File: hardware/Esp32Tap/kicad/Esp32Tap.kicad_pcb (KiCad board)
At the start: 4 copper layers, 100 x 55 mm, 93 parts, among them J1 RJ45_Console_54602-908LF, J2 RJ45_Motor_54602-908LF, J3 USB-C_HRO_TYPE-C-31-M-12, K1 G6K-2F-Y-TR DC5, Q1 BC817-40,215, Q2 2N7002, SW1 KMR2-EN, SW2 KMR2-BOOT, U1 ESP32-S3-WROOM-1-N8, U2 TPS54202DDCR, U3 USBLC6-2SC6, U4 TPS3700DDCR, U5 TPS70950DBVR, U6 SN74LVC2G08DCTR, U7 SN74LVC1G126DBVR

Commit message: hardware: clear residual JLC DFM findings
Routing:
- net PIN4_PASS: track 39.1 -> 36.0 mm, vias 4 -> 3
- net PIN3: track 110.3 -> 108.1 mm
- net EN: track 100.5 -> 102.0 mm, vias 9 -> 8

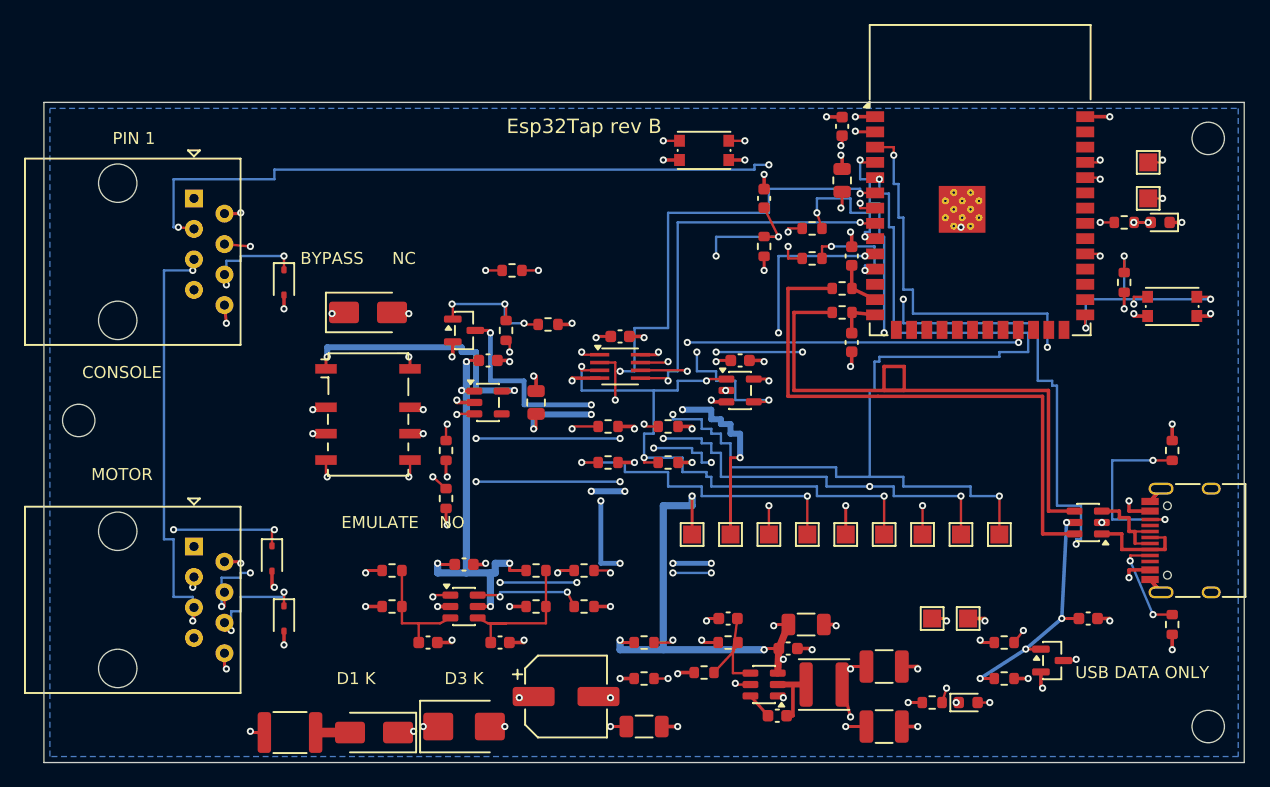
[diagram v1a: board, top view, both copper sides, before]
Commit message: hardware: publish body-safe fabrication legend
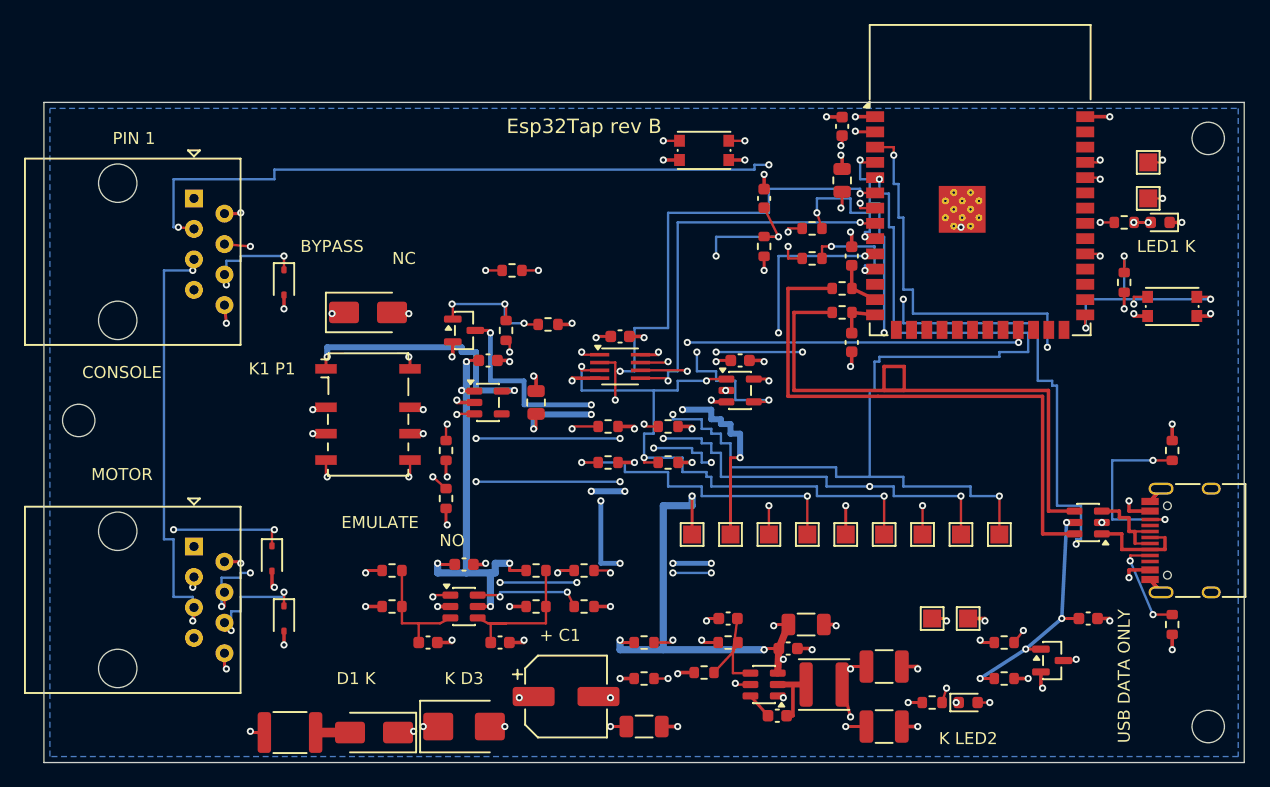
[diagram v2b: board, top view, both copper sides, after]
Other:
- board text added: "+ C1"
- board text added: "K D3"
- board text added: "K LED2"
- board text added: "K1 P1"
- board text added: "LED1 K"
- board text removed: "D3 K"
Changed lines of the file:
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@@
+		)
+	)
+	(gr_text "K1 P1"
+		(at 119 122.2 0)
+		(layer "F.SilkS")
+		(effects
+			(font
+				(size 1 1)
+				(thickness 0.2)
+			)
 		)
 	)
 	(gr_text "BYPASS"
-		(at 124 113 0)
+		(at 124 112 0)
 		(layer "F.SilkS")
 		(effects
@@
 	)
 	(gr_text "NO"
-		(at 134 135 0)
+		(at 134 136.5 0)
 		(layer "F.SilkS")
 		(effects
@@
 		)
 	)
-	(gr_text "D3 K"
+	(gr_text "K D3"
 		(at 135 148 0)
 		(layer "F.SilkS")
@@
 		)
 	)
-	(gr_text "USB DATA ONLY"
-		(at 191.5 147.5 0)
+	(gr_text "+ C1"
+		(at 143 144.4 0)
 		(layer "F.SilkS")
 		(effects
+			(font
+				(size 1 1)
+				(thickness 0.2)
+			)
+		)
+	)
+	(gr_text "K LED2"
+		(at 177 153 0)
+		(layer "F.SilkS")
+		(effects
+			(font
+				(size 1 1)
+				(thickness 0.2)
+			)
+		)
+	)
+	(gr_text "LED1 K"
+		(at 193.5 112 0)
+		(layer "F.SilkS")
+		(effects
+			(font
+				(size 1 1)
+				(thickness 0.2)
+			)
+		)
+	)
+	(gr_text "USB DATA ONLY"
+		(at 190 147.8 90)
+		(layer "F.SilkS")
+		(effects

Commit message: hardware: redesign Esp32Tap as compact turnkey Rev C (#52)
Redesign the serial-powered Esp32Tap around compact SMT Micro-Fit harness interfaces, regenerate and validate the PCB/enclosure/manufacturing package, and add fail-closed evidence, ngspice, vendor, and handoff documentation.

The hardware remains HOLD pending live JLC process/quote confirmation and physical installed measurements.
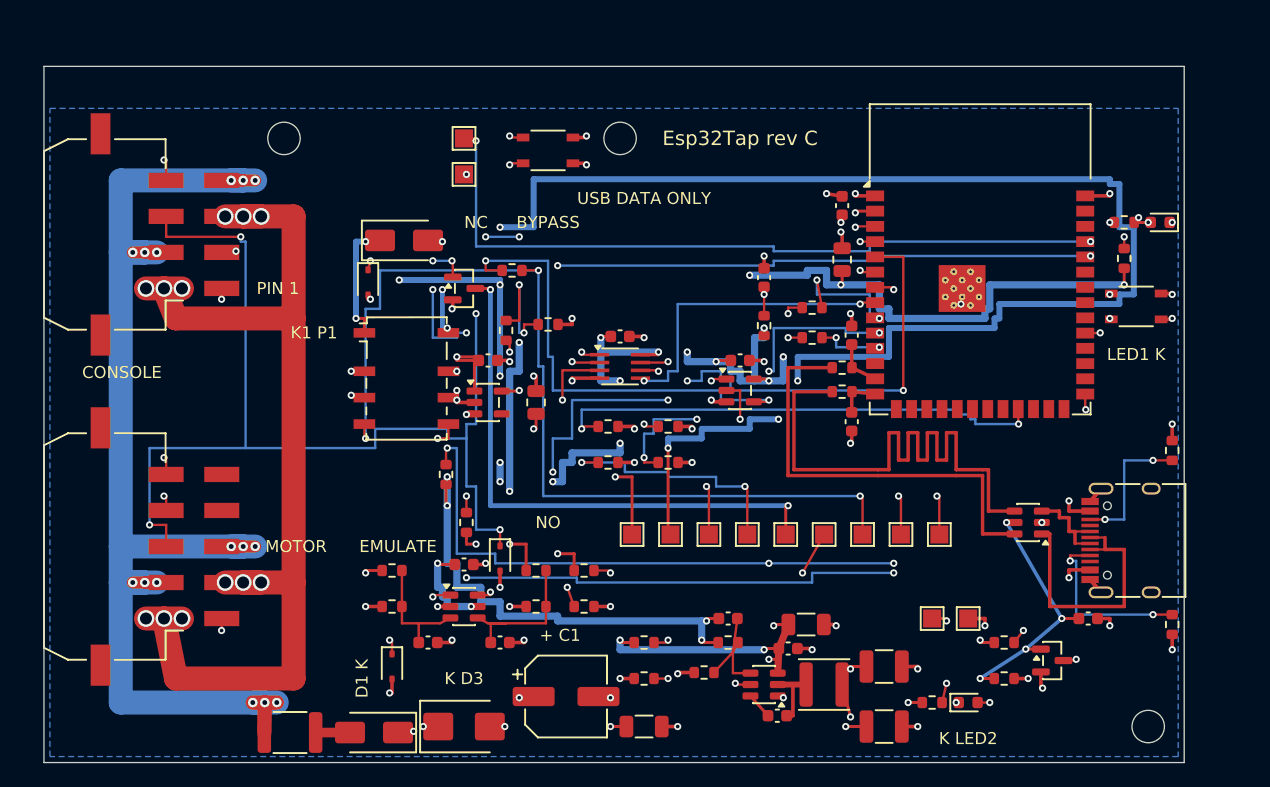
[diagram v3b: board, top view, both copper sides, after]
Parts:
- J1: value RJ45_Console_54602-908LF -> 430450809; footprint Connector_RJ:RJ45_Amphenol_54602-x08_Horizontal -> Connector_Molex:Molex_Micro-Fit_3.0_43045-0809_2x04-1MP_P3.00mm_Horizontal
- J2: value RJ45_Motor_54602-908LF -> 430451010; footprint Connector_RJ:RJ45_Amphenol_54602-x08_Horizontal -> Connector_Molex:Molex_Micro-Fit_3.0_43045-1010_2x05-1MP_P3.00mm_Horizontal
- SW1: value KMR2-EN -> SKRPACE010; footprint Button_Switch_SMD:SW_Push_1P1T_NO_CK_KMR2 -> Button_Switch_SMD:SW_SPST_SKRPACE010
- SW2: value KMR2-BOOT -> SKRPACE010; footprint Button_Switch_SMD:SW_Push_1P1T_NO_CK_KMR2 -> Button_Switch_SMD:SW_SPST_SKRPACE010
- moved TP1 57.0 mm to (135.0, 103.0)
- moved TP2 57.0 mm to (135.0, 106.0)
- moved MH2 49.0 mm to (148.0, 103.0)
- moved MH1 29.1 mm to (120.0, 103.0)
- moved D7 19.0 mm to (138.0, 138.0)
- moved SW1 13.0 mm to (142.0, 104.0)
- moved D6 9.85 mm to (129.0, 147.0)
- moved D5 7.00 mm to (127.0, 115.0)
- moved D4 6.71 mm to (130.0, 111.5)
- moved C13 6.60 mm to (167.3, 119.4)
- moved C10 6.60 mm to (160.0, 114.6)
- moved C14 6.60 mm to (167.3, 126.6)
- moved C8 6.60 mm to (166.5, 113.1)
- moved C9 6.60 mm to (166.5, 108.6)
- moved R13 6.60 mm to (160.0, 118.6)
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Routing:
- net GND: track 77.4 -> 178.0 mm, vias 55 -> 67
- net +5V_RLY: track 76.4 -> 173.2 mm, vias 9 -> 11
- net U0TXD: track 8.05 -> 62.8 mm
- net +8V_RAW: track 56.0 -> 109.5 mm, vias 5 -> 15
- net U0RXD: track 9.38 -> 61.1 mm, vias 2 -> 5
- net EN: track 102.0 -> 54.2 mm, vias 8 -> 4
- net +3V3: track 200.9 -> 238.4 mm, vias 20 -> 29
- net TX_DRV: track 106.5 -> 80.1 mm, vias 7 -> 3
- net VIN: track 133.9 -> 159.2 mm, vias 15 -> 16
- net VBUS_PRESENT_N: track 69.7 -> 45.9 mm, vias 5 -> 3
- net TREAD_OK: track 112.2 -> 91.3 mm, vias 11 -> 8
- net Q1_B: track 11.7 -> 27.8 mm, vias 3 -> 6
- net PIN5_SAFETY: track 36.2 -> 20.5 mm
- net K1_NC_FB: track 89.8 -> 102.8 mm, vias 9 -> 6
- net USB_DN: track 10.1 -> 22.8 mm
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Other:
- board size 100 x 55 mm -> 95 x 58 mm
- board text added: "Esp32Tap rev C"
- board text removed: "Esp32Tap rev B"
